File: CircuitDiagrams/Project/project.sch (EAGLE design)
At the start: 123 parts, among them IC1 UC3C, IC2 PCA9542A, IC3 MT48LC4M16A2TSOP54, IC4 TB6593FNGSSOP20, IC5 TB6593FNGSSOP20, J2 1BY2THROUGHHOLE, J3 1BY2THROUGHHOLE, J4 1BY2THROUGHHOLE, J5 8PIN1.27MM2X4TH, J6 4PIN1.27MM2X2TH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

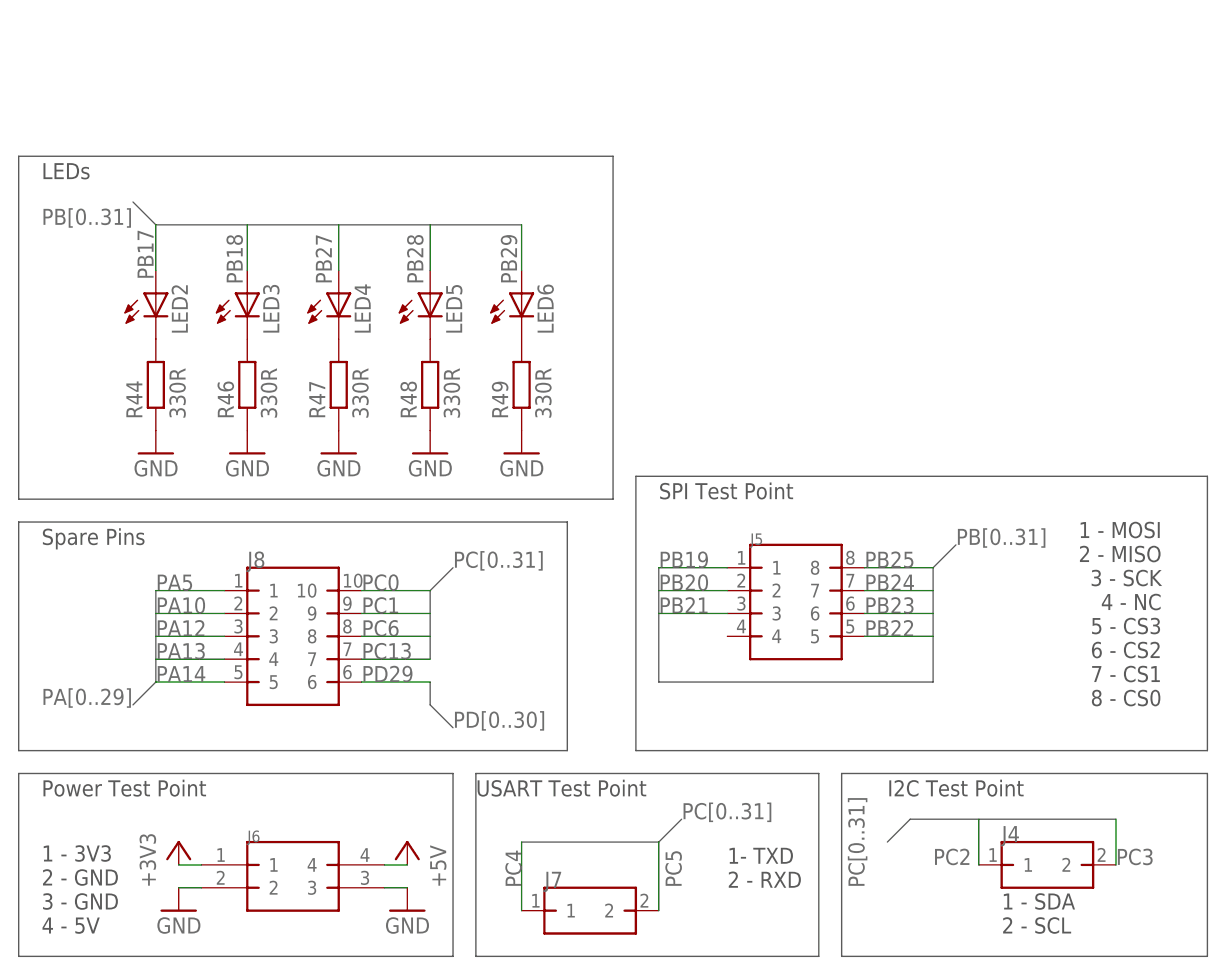
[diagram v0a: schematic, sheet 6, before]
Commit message: Changed the JTAG Package. Added Headers for all unused pins.
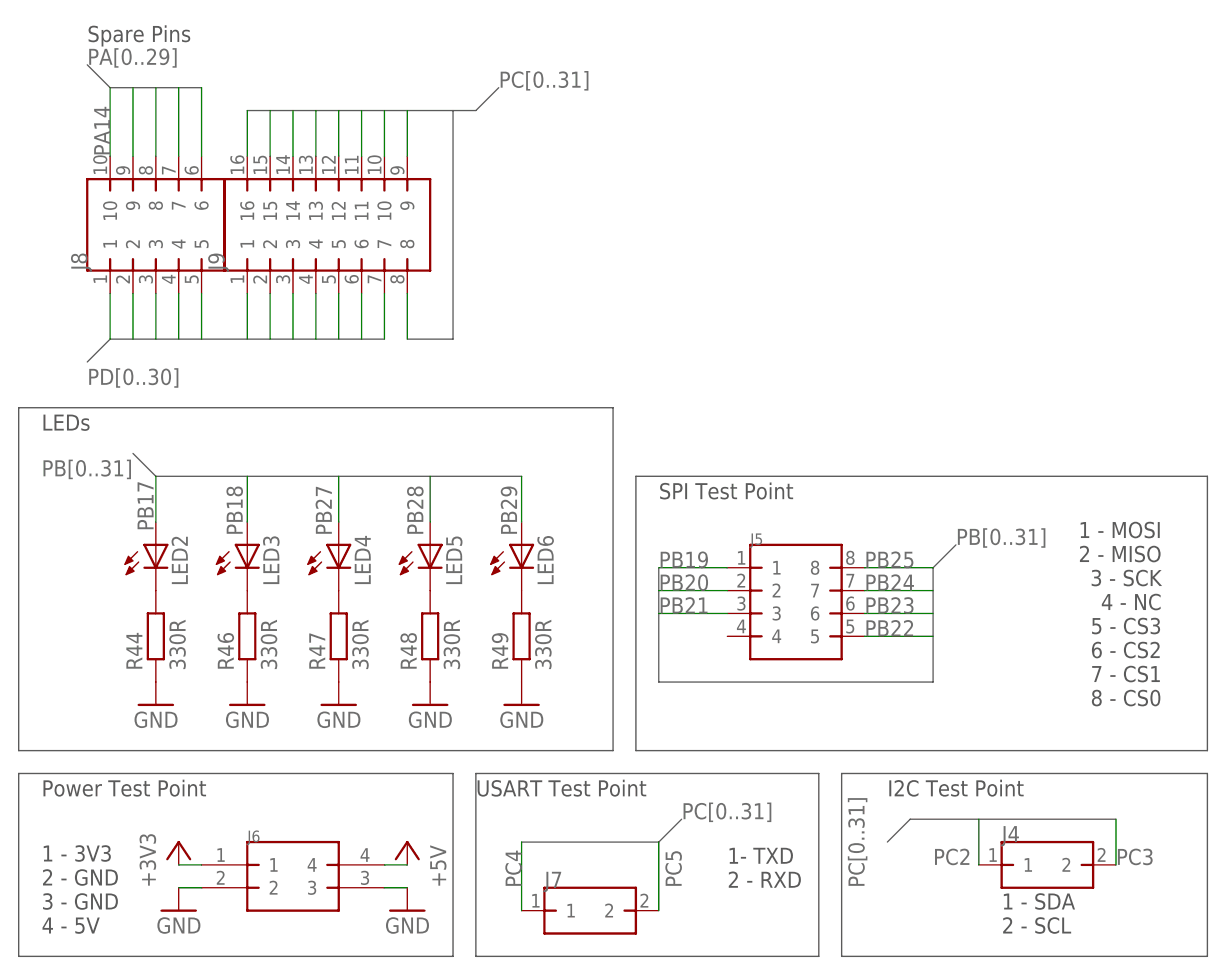
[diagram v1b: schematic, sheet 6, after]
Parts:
- added J9: 16PIN2.54MM2X8TH, Headers:16PIN2.54MM2X8TH
- J1: value (none) -> JTAG2.54MM2X5TH; device Headers:JTAG -> Headers:JTAG2.54MM2X5TH
- J5: value 8PIN1.27MM2X4TH -> 8PIN2.54MM1X8TH; device Headers:8PIN1.27MM2X4TH -> Headers:8PIN2.54MM1X8TH
- J6: value 4PIN1.27MM2X2TH -> 4PIN2.54MM2X2TH; device Headers:4PIN1.27MM2X2TH -> Headers:4PIN2.54MM2X2TH
- J8: value 10PIN1.27MM2X5TH -> 10PIN2.54MM2X5TH; device Headers:10PIN1.27MM2X5TH -> Headers:10PIN2.54MM2X5TH
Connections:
- net PA10: now also J8.7; no longer J8.2
- net PA12: now also J8.8; no longer J8.3
- net PA13: now also J8.9; no longer J8.4
- net PA14: now also J8.10; no longer J8.5
- net PA5: now also J8.6; no longer J8.1
- net PC0: now also J9.16; no longer J8.10
- net PC1: now also J9.15; no longer J8.9
- net PC10: now also J9.11
- net PC11: now also J9.10
- net PC12: now also J9.9
- net PC13: now also J9.8; no longer J8.7
- net PC6: now also J9.14; no longer J8.8
- net PC7: now also J9.13
- net PC9: now also J9.12
- net PD16: now also J8.2
- net PD18: now also J8.3
- net PD19: now also J8.4
- net PD22: now also J8.5
- net PD23: now also J9.1
- net PD25: now also J9.2
- net PD26: now also J9.3
- net PD27: now also J9.4
- net PD28: now also J9.5
- net PD29: now also J9.6; no longer J8.6
- net PD30: now also J9.7
- net PD4: now also J8.1
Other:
- moved on the sheet: J8, LED2, LED3, LED4, LED5, LED6, R44, R46, R47, R48, R49

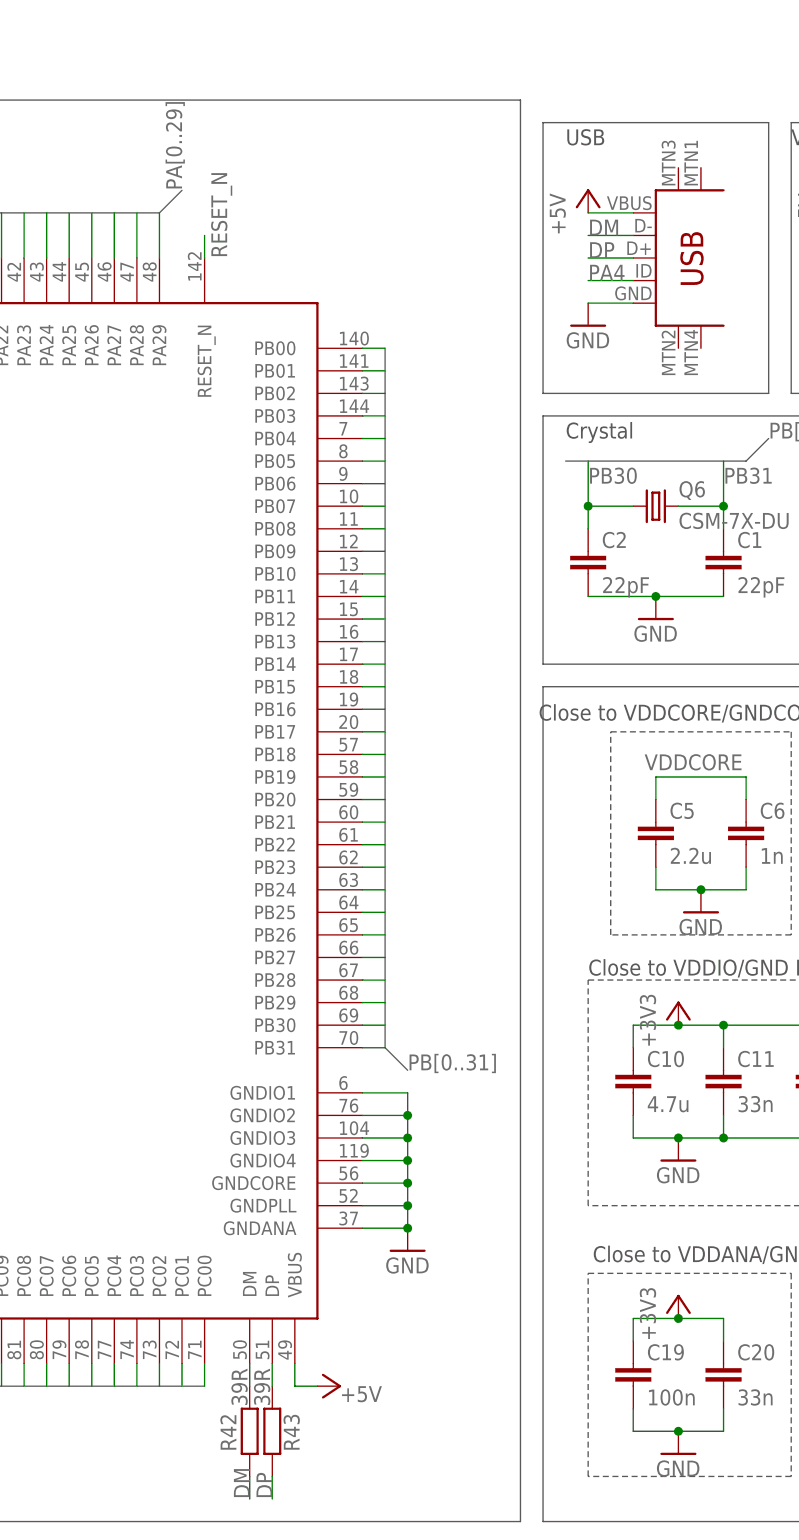
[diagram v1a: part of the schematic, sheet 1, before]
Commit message: Routed all +3V3 signals. Made into a four layer board.
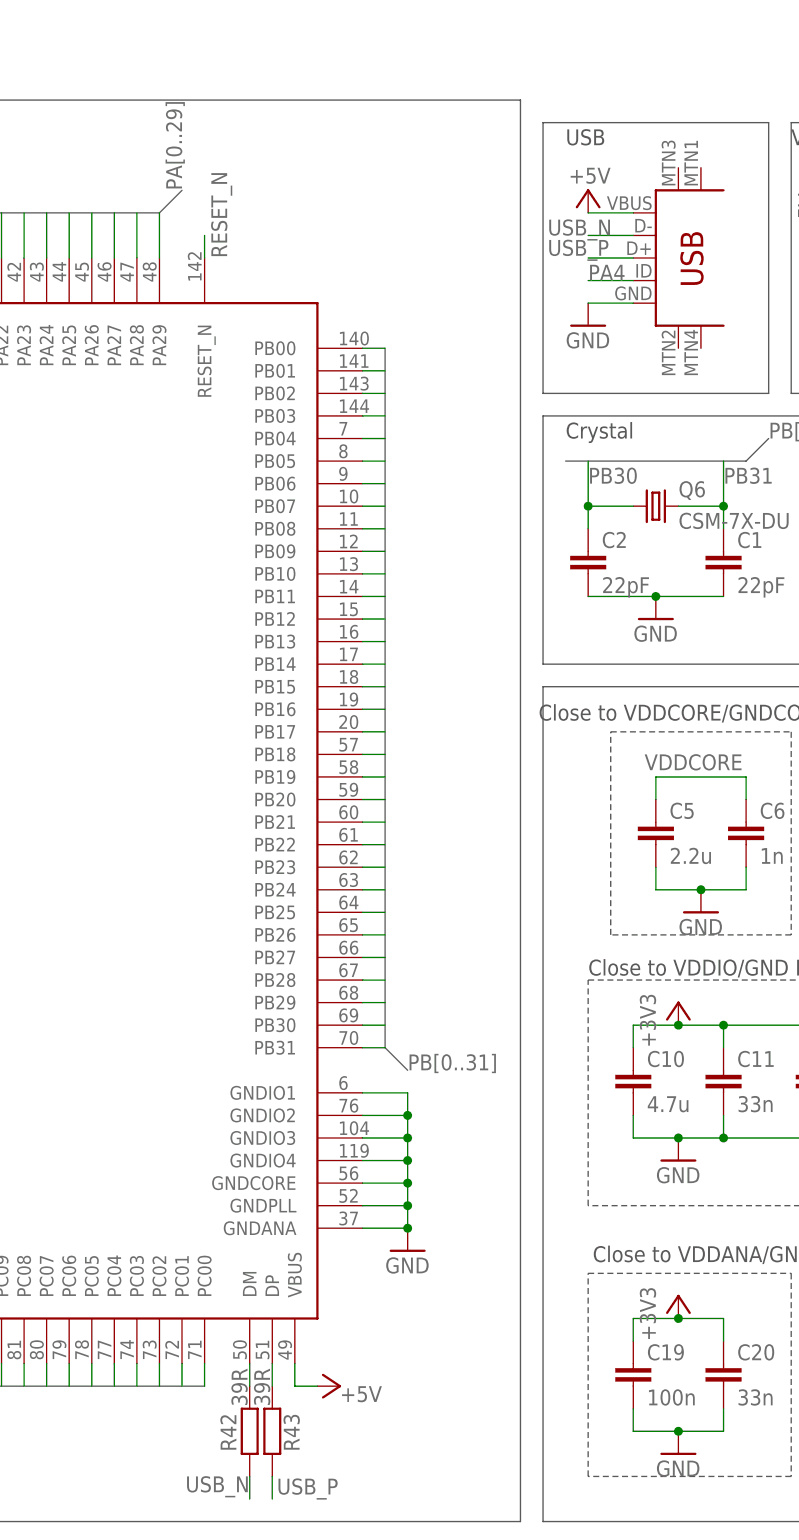
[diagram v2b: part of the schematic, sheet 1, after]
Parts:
- J5: value 8PIN2.54MM1X8TH -> 8PIN2.54MM2X4TH; device Headers:8PIN2.54MM1X8TH -> Headers:8PIN2.54MM2X4TH
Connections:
- net DM renamed USB_N
- net DP renamed USB_P
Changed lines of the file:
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@@
 <grid distance="0.1" unitdist="inch" unit="inch" style="lines" multiple="1" display="no" altdistance="0.01" altunitdist="inch" altunit="inch"/>
 <layers>
-<layer number="1" name="Top" color="4" fill="1" visible="no" active="no"/>
-<layer number="2" name="Route2" color="3" fill="1" visible="no" active="no"/>
-<layer number="3" name="Route3" color="13" fill="1" visible="no" active="no"/>
-<layer number="14" name="Route14" color="1" fill="6" visible="no" active="no"/>
-<layer number="15" name="Route15" color="4" fill="6" visible="no" active="no"/>
-<layer number="16" name="Bottom" color="1" fill="1" visible="no" active="no"/>
-<layer number="17" name="Pads" color="2" fill="1" visible="no" active="no"/>
-<layer number="18" name="Vias" color="2" fill="1" visible="no" active="no"/>
-<layer number="19" name="Unrouted" color="6" fill="1" visible="no" active="no"/>
-<layer number="20" name="Dimension" color="15" fill="1" visible="no" active="no"/>
-<layer number="21" name="tPlace" color="7" fill="1" visible="no" active="no"/>
-<layer number="22" name="bPlace" color="7" fill="1" visible="no" active="no"/>
-<layer number="23" name="tOrigins" color="15" fill="1" visible="no" active="no"/>
-<layer number="24" name="bOrigins" color="15" fill="1" visible="no" active="no"/>
-<layer number="25" name="tNames" color="7" fill="1" visible="no" active="no"/>
-<layer number="26" name="bNames" color="7" fill="1" visible="no" active="no"/>
-<layer number="27" name="tValues" color="7" fill="1" visible="no" active="no"/>
-<layer number="28" name="bValues" color="7" fill="1" visible="no" active="no"/>
+<layer number="1" name="Top" color="4" fill="1" visible="yes" active="no"/>
+<layer number="2" name="Route2" color="1" fill="3" visible="yes" active="no"/>
+<layer number="3" name="Route3" color="4" fill="3" visible="yes" active="no"/>
+<layer number="14" name="Route14" color="1" fill="6" visible="yes" active="no"/>
+<layer number="15" name="Route15" color="4" fill="6" visible="yes" active="no"/>
+<layer number="16" name="Bottom" color="1" fill="1" visible="yes" active="no"/>
+<layer number="17" name="Pads" color="2" fill="1" visible="yes" active="no"/>
+<layer number="18" name="Vias" color="2" fill="1" visible="yes" active="no"/>
+<layer number="19" name="Unrouted" color="6" fill="1" visible="yes" active="no"/>
+<layer number="20" name="Dimension" color="15" fill="1" visible="yes" active="no"/>
+<layer number="21" name="tPlace" color="7" fill="1" visible="yes" active="no"/>
+<layer number="22" name="bPlace" color="7" fill="1" visible="yes" active="no"/>
+<layer number="23" name="tOrigins" color="15" fill="1" visible="yes" active="no"/>
+<layer number="24" name="bOrigins" color="15" fill="1" visible="yes" active="no"/>
+<layer number="25" name="tNames" color="7" fill="1" visible="yes" active="no"/>
+<layer number="26" name="bNames" color="7" fill="1" visible="yes" active="no"/>
+<layer number="27" name="tValues" color="7" fill="1" visible="yes" active="no"/>
+<layer number="28" name="bValues" color="7" fill="1" visible="yes" active="no"/>
 <layer number="29" name="tStop" color="7" fill="3" visible="no" active="no"/>
 <layer number="30" name="bStop" color="7" fill="6" visible="no" active="no"/>
@@
 <layer number="35" name="tGlue" color="7" fill="4" visible="no" active="no"/>
 <layer number="36" name="bGlue" color="7" fill="5" visible="no" active="no"/>
-<layer number="37" name="tTest" color="7" fill="1" visible="no" active="no"/>
-<layer number="38" name="bTest" color="7" fill="1" visible="no" active="no"/>
+<layer number="37" name="tTest" color="7" fill="1" visible="yes" active="no"/>
+<layer number="38" name="bTest" color="7" fill="1" visible="yes" active="no"/>
 <layer number="39" name="tKeepout" color="4" fill="11" visible="no" active="no"/>
 <layer number="40" name="bKeepout" color="1" fill="11" visible="no" active="no"/>
@@
 <layer number="44" name="Drills" color="7" fill="1" visible="no" active="no"/>
 <layer number="45" name="Holes" color="7" fill="1" visible="no" active="no"/>
-<layer number="46" name="Milling" color="3" fill="1" visible="no" active="no"/>
-<layer number="47" name="Measures" color="7" fill="1" visible="no" active="no"/>
-<layer number="48" name="Document" color="7" fill="1" visible="no" active="no"/>
-<layer number="49" name="Reference" color="7" fill="1" visible="no" active="no"/>
-<layer number="50" name="dxf" color="7" fill="1" visible="no" active="no"/>
-<layer number="51" name="tDocu" color="7" fill="1" visible="no" active="no"/>
-<layer number="52" name="bDocu" color="7" fill="1" visible="no" active="no"/>
-<layer number="53" name="tGND_GNDA" color="7" fill="9" visible="no" active="no"/>
-<layer number="54" name="bGND_GNDA" color="1" fill="9" visible="no" active="no"/>
-<layer number="56" name="wert" color="7" fill="1" visible="no" active="no"/>
+<layer number="46" name="Milling" color="3" fill="1" visible="yes" active="no"/>
+<layer number="47" name="Measures" color="7" fill="1" visible="yes" active="no"/>
+<layer number="48" name="Document" color="7" fill="1" visible="yes" active="no"/>
+<layer number="49" name="Reference" color="7" fill="1" visible="yes" active="no"/>
+<layer number="50" name="dxf" color="7" fill="1" visible="yes" active="no"/>
+<layer number="51" name="tDocu" color="7" fill="1" visible="yes" active="no"/>
+<layer number="52" name="bDocu" color="7" fill="1" visible="yes" active="no"/>
+<layer number="53" name="tGND_GNDA" color="7" fill="9" visible="yes" active="no"/>
+<layer number="54" name="bGND_GNDA" color="1" fill="9" visible="yes" active="no"/>
+<layer number="56" name="wert" color="7" fill="1" visible="yes" active="no"/>
 <layer number="91" name="Nets" color="2" fill="1" visible="yes" active="yes"/>
 <layer number="92" name="Busses" color="1" fill="1" visible="yes" active="yes"/>
@@
 <part name="+3V38" library="supply1" deviceset="+3V3" device=""/>
 <part name="GND37" library="supply1" deviceset="GND" device=""/>
-<part name="J5" library="Headers" deviceset="8PIN" device="2.54MM1X8TH"/>
+<part name="J5" library="Headers" deviceset="8PIN" device="2.54MM2X4TH" value="8PIN2.54MM2X4TH"/>
 <part name="J6" library="Headers" deviceset="4PIN" device="2.54MM2X2TH"/>
 <part name="+3V39" library="supply1" deviceset="+3V3" device=""/>
@@
 <attribute name="VALUE" x="106.68" y="-7.62" size="1.778" layer="96" rot="MR180"/>
 </instance>
-<instance part="P+3" gate="1" x="134.62" y="127"/>
+<instance part="P+3" gate="1" x="134.62" y="127" smashed="yes">
+<attribute name="VALUE" x="137.16" y="129.54" size="1.778" layer="96" rot="R180"/>
+</instance>
 <instance part="Q6" gate="P" x="142.24" y="91.44"/>
 <instance part="GND19" gate="1" x="142.24" y="78.74"/>
@@
 </segment>
 </net>
-<net name="DP" class="0">
+<net name="USB_P" class="0">
 <segment>
 <pinref part="U$1" gate="G$1" pin="D+"/>
 <wire x1="139.7" y1="119.38" x2="134.62" y2="119.38" width="0.1524" layer="91"/>
-<label x="134.62" y="119.38" size="1.778" layer="95"/>
+<label x="130.048" y="119.634" size="1.778" layer="95"/>
 </segment>
 <segment>
 <pinref part="R43" gate="G$1" pin="1"/>
 <wire x1="99.06" y1="-17.78" x2="99.06" y2="-20.32" width="0.1524" layer="91"/>
-<label x="99.06" y="-20.32" size="1.778" layer="95" rot="R90"/>
-</segment>
-</net>
-<net name="DM" class="0">
+<label x="99.568" y="-19.812" size="1.778" layer="95"/>
+</segment>
+</net>
+<net name="USB_N" class="0">
 <segment>
 <pinref part="U$1" gate="G$1" pin="D-"/>
 <wire x1="139.7" y1="121.92" x2="134.62" y2="121.92" width="0.1524" layer="91"/>
-<label x="134.62" y="121.92" size="1.778" layer="95"/>
+<label x="130.048" y="121.92" size="1.778" layer="95"/>
 </segment>
 <segment>
 <pinref part="R42" gate="G$1" pin="1"/>
 <wire x1="96.52" y1="-17.78" x2="96.52" y2="-20.32" width="0.1524" layer="91"/>
-<label x="96.52" y="-20.32" size="1.778" layer="95" rot="R90"/>
-</segment>
-</net>
+<label x="96.52" y="-17.78" size="1.778" layer="95" rot="R180"/>
+</segment>
+</net>

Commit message: Finished Wiring GND. Done USB Data and oscillator
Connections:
- net N$28 renamed DATA_N
- net N$29 renamed DATA_P
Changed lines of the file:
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@@
 </segment>
 </net>
-<net name="N$28" class="0">
+<net name="DATA_N" class="0">
 <segment>
 <pinref part="IC1" gate="G$1" pin="DM"/>
@@
 </segment>
 </net>
-<net name="N$29" class="0">
+<net name="DATA_P" class="0">
 <segment>
 <pinref part="IC1" gate="G$1" pin="DP"/>

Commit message: Routed DQ Lines on the SDRAM.
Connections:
- net N$10 renamed DQ03
- net N$11 renamed DQ04
- net N$12 renamed DQ05
- net N$13 renamed DQ06
- net N$14 renamed DQ07
- net N$15 renamed DQ08
- net N$16 renamed DQ09
- net N$17 renamed DQ10
- net N$18 renamed DQ11
- net N$19 renamed DQ12
- net N$20 renamed DQ13
- net N$21 renamed DQ14
- net N$22 renamed DQ15
- net N$7 renamed DQ00
- net N$8 renamed DQ01
- net N$9 renamed DQ02
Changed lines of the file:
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@@
 </segment>
 </net>
-<net name="N$7" class="0">
+<net name="DQ00" class="0">
 <segment>
 <pinref part="IC3" gate="G$1" pin="DQ00"/>
@@
 </segment>
 </net>
-<net name="N$8" class="0">
+<net name="DQ01" class="0">
 <segment>
 <pinref part="IC3" gate="G$1" pin="DQ01"/>
@@
 </segment>
 </net>
-<net name="N$9" class="0">
+<net name="DQ02" class="0">
 <segment>
 <pinref part="IC3" gate="G$1" pin="DQ02"/>
@@
 </segment>
 </net>
-<net name="N$10" class="0">
+<net name="DQ03" class="0">
 <segment>
 <pinref part="IC3" gate="G$1" pin="DQ03"/>
@@
 </segment>
 </net>
-<net name="N$11" class="0">
+<net name="DQ04" class="0">
 <segment>
 <pinref part="IC3" gate="G$1" pin="DQ04"/>
@@
 </segment>
 </net>
-<net name="N$12" class="0">
+<net name="DQ05" class="0">
 <segment>
 <pinref part="IC3" gate="G$1" pin="DQ05"/>
@@
 </segment>
 </net>
-<net name="N$13" class="0">
+<net name="DQ06" class="0">
 <segment>
 <pinref part="IC3" gate="G$1" pin="DQ06"/>
@@
 </segment>
 </net>
-<net name="N$14" class="0">
+<net name="DQ07" class="0">
 <segment>
 <pinref part="IC3" gate="G$1" pin="DQ07"/>
@@
 </segment>
 </net>
-<net name="N$15" class="0">
+<net name="DQ08" class="0">
 <segment>
 <pinref part="IC3" gate="G$1" pin="DQ08"/>
@@
 </segment>
 </net>
-<net name="N$16" class="0">
+<net name="DQ09" class="0">
 <segment>
 <pinref part="IC3" gate="G$1" pin="DQ09"/>
@@
 </segment>
 </net>
-<net name="N$17" class="0">
+<net name="DQ10" class="0">
 <segment>
 <pinref part="IC3" gate="G$1" pin="DQ10"/>
@@
 </segment>
 </net>
-<net name="N$18" class="0">
+<net name="DQ11" class="0">
 <segment>
 <pinref part="IC3" gate="G$1" pin="DQ11"/>
@@
 </segment>
 </net>
-<net name="N$19" class="0">
+<net name="DQ12" class="0">
 <segment>
 <pinref part="IC3" gate="G$1" pin="DQ12"/>
@@
 </segment>
 </net>
-<net name="N$20" class="0">
+<net name="DQ13" class="0">
 <segment>
 <pinref part="IC3" gate="G$1" pin="DQ13"/>
@@
 </segment>
 </net>
-<net name="N$21" class="0">
+<net name="DQ14" class="0">
 <segment>
 <pinref part="IC3" gate="G$1" pin="DQ14"/>
@@
 </segment>
 </net>
-<net name="N$22" class="0">
+<net name="DQ15" class="0">
 <segment>
 <pinref part="IC3" gate="G$1" pin="DQ15"/>

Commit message: Ripped up SDRAM lines due to poor routing. Working on it again
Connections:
- net N$24 renamed SDRAMCLK
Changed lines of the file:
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@@
 </segment>
 </net>
-<net name="N$24" class="0">
+<net name="SDRAMCLK" class="0">
 <segment>
 <pinref part="R33" gate="G$1" pin="2"/>
